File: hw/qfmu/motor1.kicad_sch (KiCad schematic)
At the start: 3 parts, among them U12 TLP2366V4-TPL_E, U3 FAN7888, U7 IMC101TT038XUMA1

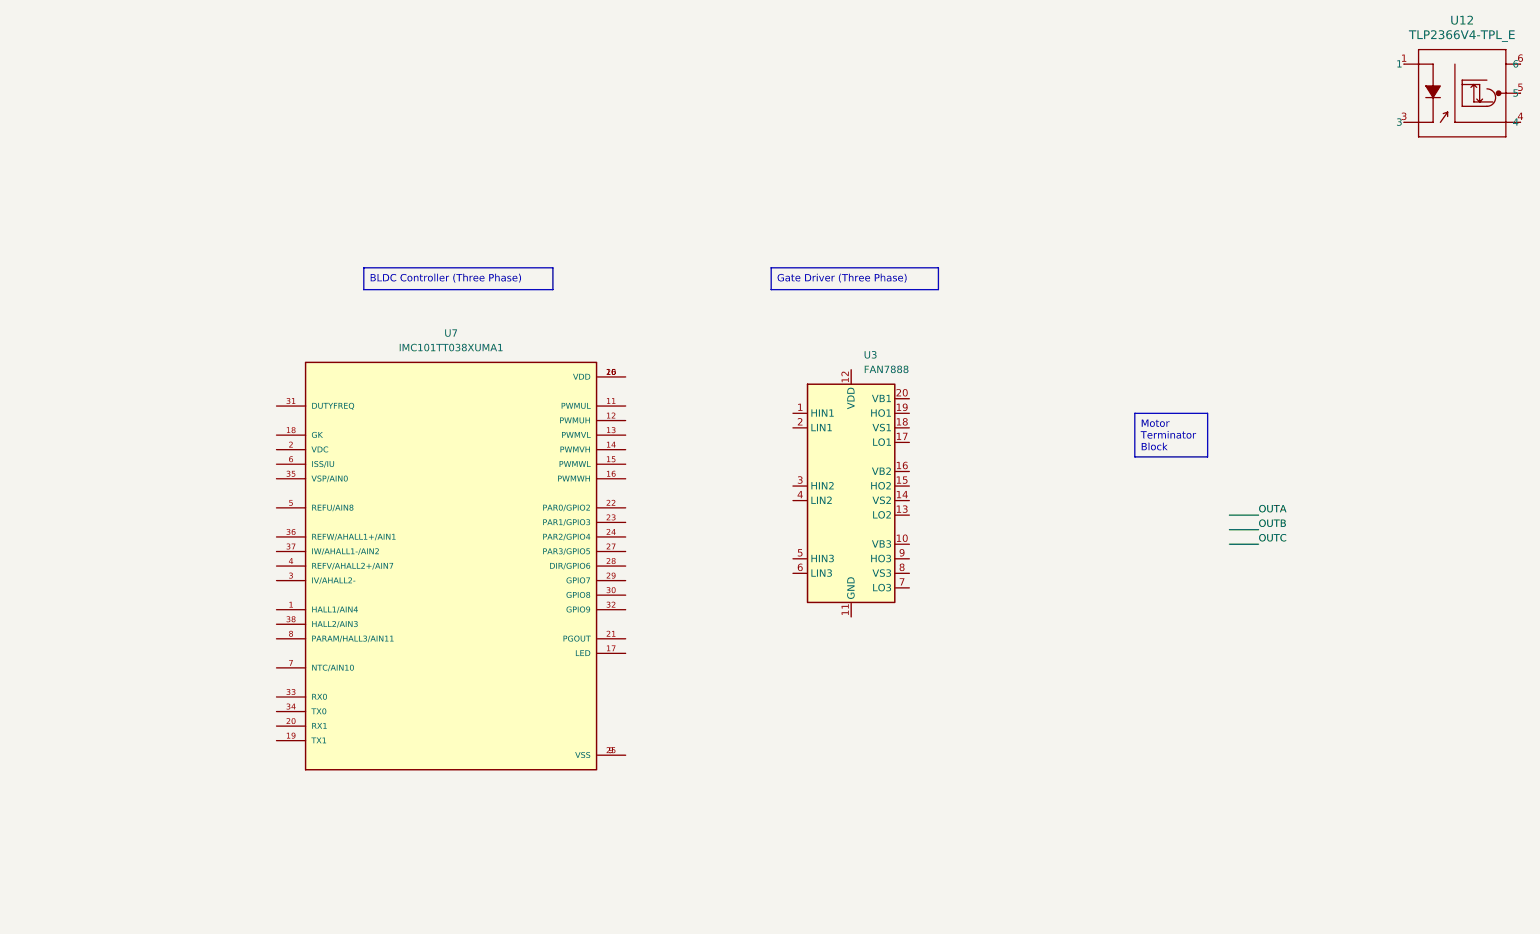
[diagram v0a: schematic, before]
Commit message: feat: add new BLDC controler and RF section
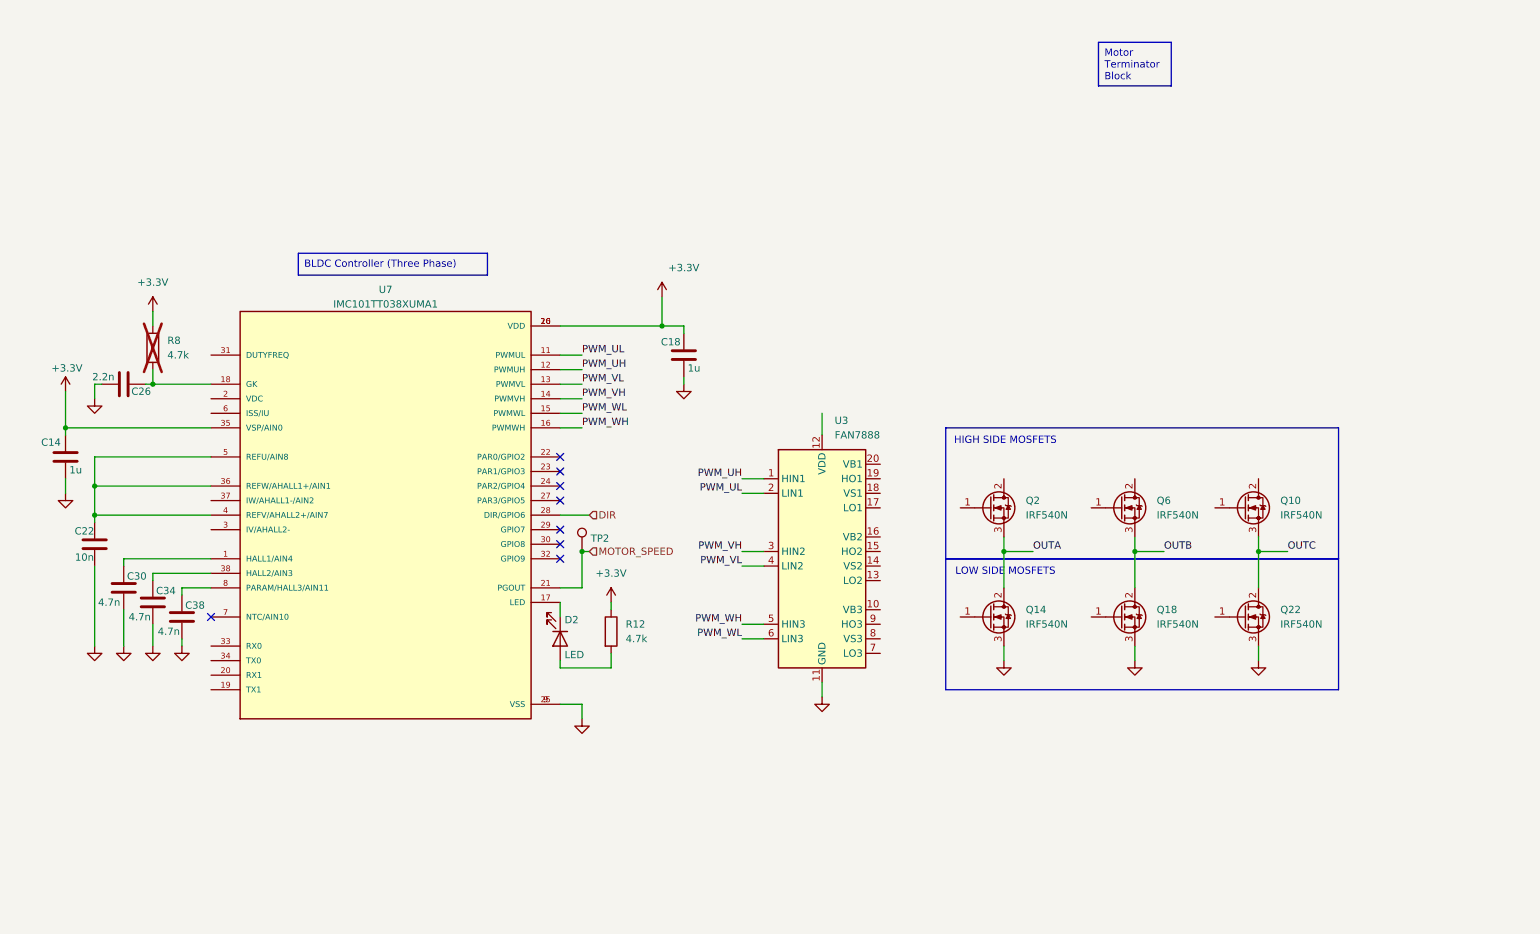
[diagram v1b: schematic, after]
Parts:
- removed U12: TLP2366V4-TPL_E, 5pin SO6_TOS, symbol TLP2366_V4_TPL_E:TLP2366V4-TPL_E
- added C14, C18: 1u, Capacitor_SMD:C_0805_2012Metric_Pad1.18x1.45mm_HandSolder, symbol Device:C
- added C22: 10n, Capacitor_SMD:C_0805_2012Metric_Pad1.18x1.45mm_HandSolder, symbol Device:C
- added C26: 2.2n, Capacitor_SMD:C_0805_2012Metric_Pad1.18x1.45mm_HandSolder, symbol Device:C
- added C30, C34, C38: 4.7n, Capacitor_SMD:C_0805_2012Metric_Pad1.18x1.45mm_HandSolder, symbol Device:C
- added D2: LED, LED_SMD:LED_1206_3216Metric_Pad1.42x1.75mm_HandSolder, symbol Device:LED
- added Q10, Q14, Q18, Q2, Q22, Q6: IRF540N, Package_TO_SOT_THT:TO-220-3_Horizontal_TabDown, symbol Transistor_FET:IRF540N
- added R12, R8: 4.7k, Resistor_SMD:R_0805_2012Metric_Pad1.20x1.40mm_HandSolder, symbol Device:R
- added TP2: TestPoint, Connector_Pin:Pin_D0.7mm_L6.5mm_W1.8mm_FlatFork, symbol Connector:TestPoint
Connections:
- net OUTA: now also Q14.2 (D), Q2.3 (S)
- net OUTB: now also Q18.2 (D), Q6.3 (S)
- net OUTC: now also Q10.3 (S), Q22.2 (D)
- net PWM_UH: now reaches U3.1 (HIN1)
- net PWM_UH: now also U7.12 (PWMUH)
- net GND: now reaches U3.11 (GND)
- net GND: now also U7.25 (VSS), U7.9 (VSS), C14.2, C18.2, C22.2, C26.1, C30.2, C34.2, C38.2, Q14.3 (S), Q18.3 (S), Q22.3 (S)
- net PWM_UL: now reaches U3.2 (LIN1)
- net PWM_UL: now also U7.11 (PWMUL)
- net PWM_VH: now reaches U3.3 (HIN2)
- net PWM_VH: now also U7.14 (PWMVH)
- net PWM_VL: now reaches U3.4 (LIN2)
- net PWM_VL: now also U7.13 (PWMVL)
- net PWM_WH: now reaches U3.5 (HIN3)
- net PWM_WH: now also U7.16 (PWMWH)
- net PWM_WL: now reaches U3.6 (LIN3)
- net PWM_WL: now also U7.15 (PWMWL)
- net at U7.1 (HALL1/AIN4): now also C30.1
- net +3.3V: now reaches U7.10 (VDD), U7.26 (VDD)
- net +3.3V: now also U7.35 (VSP/AIN0), C14.1, C18.1, R12.1, R8.1
- net at U7.17 (LED): now also D2.1 (K)
- net at U7.18 (GK): now also C26.2, R8.2
- net MOTOR_SPEED: now reaches U7.21 (PGOUT)
- net MOTOR_SPEED: now also TP2.1
- net DIR: now reaches U7.28 (DIR/GPIO6)
- net at U7.36 (REFW/AHALL1+/AIN1): now also U7.4 (REFV/AHALL2+/AIN7), U7.5 (REFU/AIN8), C22.1
- net at U7.38 (HALL2/AIN3): now also C34.1
- net at U7.8 (PARAM/HALL3/AIN11): now also C38.1
- new net: D2.2 (A), R12.2
- no-connect marks 0 -> 8
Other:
- note added: "HIGH SIDE MOSFETS"
- note added: "LOW SIDE MOSFETS"
- company: Daniel Pérez -> Daniel Enrique Pérez Díaz
- title: (none) -> Quincy FMU

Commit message: feat: finish motors, RF and power monitor
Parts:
- removed U3: FAN7888, Package_SO:SOIC-20W_7.5x12.8mm_P1.27mm, symbol Driver_FET:FAN7888
- added C74: 220p, Capacitor_SMD:C_0805_2012Metric_Pad1.18x1.45mm_HandSolder, symbol Device:C
- added C77: 1u, Capacitor_SMD:C_0805_2012Metric_Pad1.18x1.45mm_HandSolder, symbol Device:C
- added C81, C85, C89: 0.1u, Capacitor_SMD:C_0805_2012Metric_Pad1.18x1.45mm_HandSolder, symbol Device:C
- added J4: Conn_01x03_Pin, Connector_Phoenix_SPT:PhoenixContact_SPT_1.5_3-H-3.5_1x03_P3.5mm_Horizontal, symbol Connector:Conn_01x03_Pin
- added R4: 1, Resistor_SMD:R_0805_2012Metric_Pad1.20x1.40mm_HandSolder, symbol Device:R
- added R44: 2k, Resistor_SMD:R_0805_2012Metric_Pad1.20x1.40mm_HandSolder, symbol Device:R
- added R48: 10k, Resistor_SMD:R_0805_2012Metric_Pad1.20x1.40mm_HandSolder, symbol Device:R
- added R51: 100k, Resistor_SMD:R_0805_2012Metric_Pad1.20x1.40mm_HandSolder, symbol Device:R
- added R55: 300k, Resistor_SMD:R_0805_2012Metric_Pad1.20x1.40mm_HandSolder, symbol Device:R
- added U2: DRV8300UDPWR, TSSOP_0DIPWR_TEX, symbol DRV8300UDPWR:DRV8300UDPWR
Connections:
- net +3.3V: now also R48.2
- net GND: now also C74.2, C77.1, R4.2, R55.1, U2.8 (GND); no longer Q14.3 (S), Q18.3 (S), Q22.3 (S)
- net OUTA: now also C81.1, J4.3 (Pin_3), U2.18 (SHA)
- net OUTB: now also C85.1, J4.2 (Pin_2), U2.15 (SHB)
- net OUTC: now also C89.1, J4.1 (Pin_1), U2.12 (SHC)
- net PWM_UH: now also U2.1 (INHA)
- net PWM_UL: now also U2.4 (INLA)
- net PWM_VH: now also U2.2 (INHB)
- net PWM_VL: now also U2.5 (INLB)
- net PWM_WH: now also U2.3 (INHC)
- net PWM_WL: now also U2.6 (INLC)
- net LO3: now reaches Q22.1 (G)
- net LO3: now also U2.10 (GLB)
- net HO3: now reaches Q10.1 (G)
- net HO3: now also U2.13 (GHC)
- net +12V: now reaches Q10.2 (D)
- net +12V: now also Q2.2 (D), Q6.2 (D), C77.2, R51.1, U2.7 (GVDD)
- net HO2: now reaches Q6.1 (G)
- net HO2: now also U2.16 (GHB)
- net LO2: now reaches Q18.1 (G)
- net LO2: now also U2.9 (GLC)
- net LO1: now reaches Q14.1 (G)
- net LO1: now also U2.11 (GLA)
- net HO1: now reaches Q2.1 (G)
- net HO1: now also U2.19 (GHA)
- net VDC: now reaches U7.2 (VDC)
- net VDC: now also R51.2, R55.2
- net DUTYFREQ: now reaches U7.31 (DUTYFREQ)
- net CONT_FW_RX0: now reaches U7.33 (RX0)
- net CONT_FW_TX0: now reaches U7.34 (TX0)
- net IU+: now reaches U7.6 (ISS/IU)
- net IU+: now also C74.1, R44.2, R48.1
- new net: Q14.3 (S), Q18.3 (S), Q22.3 (S), R4.1, R44.1
- new net BSTA: C81.2, U2.20 (BSTA)
- new net BSTB: C85.2, U2.17 (BSTB)
- new net BSTC: C89.2, U2.14 (BSTC)
- no-connect marks 8 -> 12
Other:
- moved on the sheet: C14, C18, C22, C26, C30, C34, C38, D2, Q10, Q14, Q18, Q2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

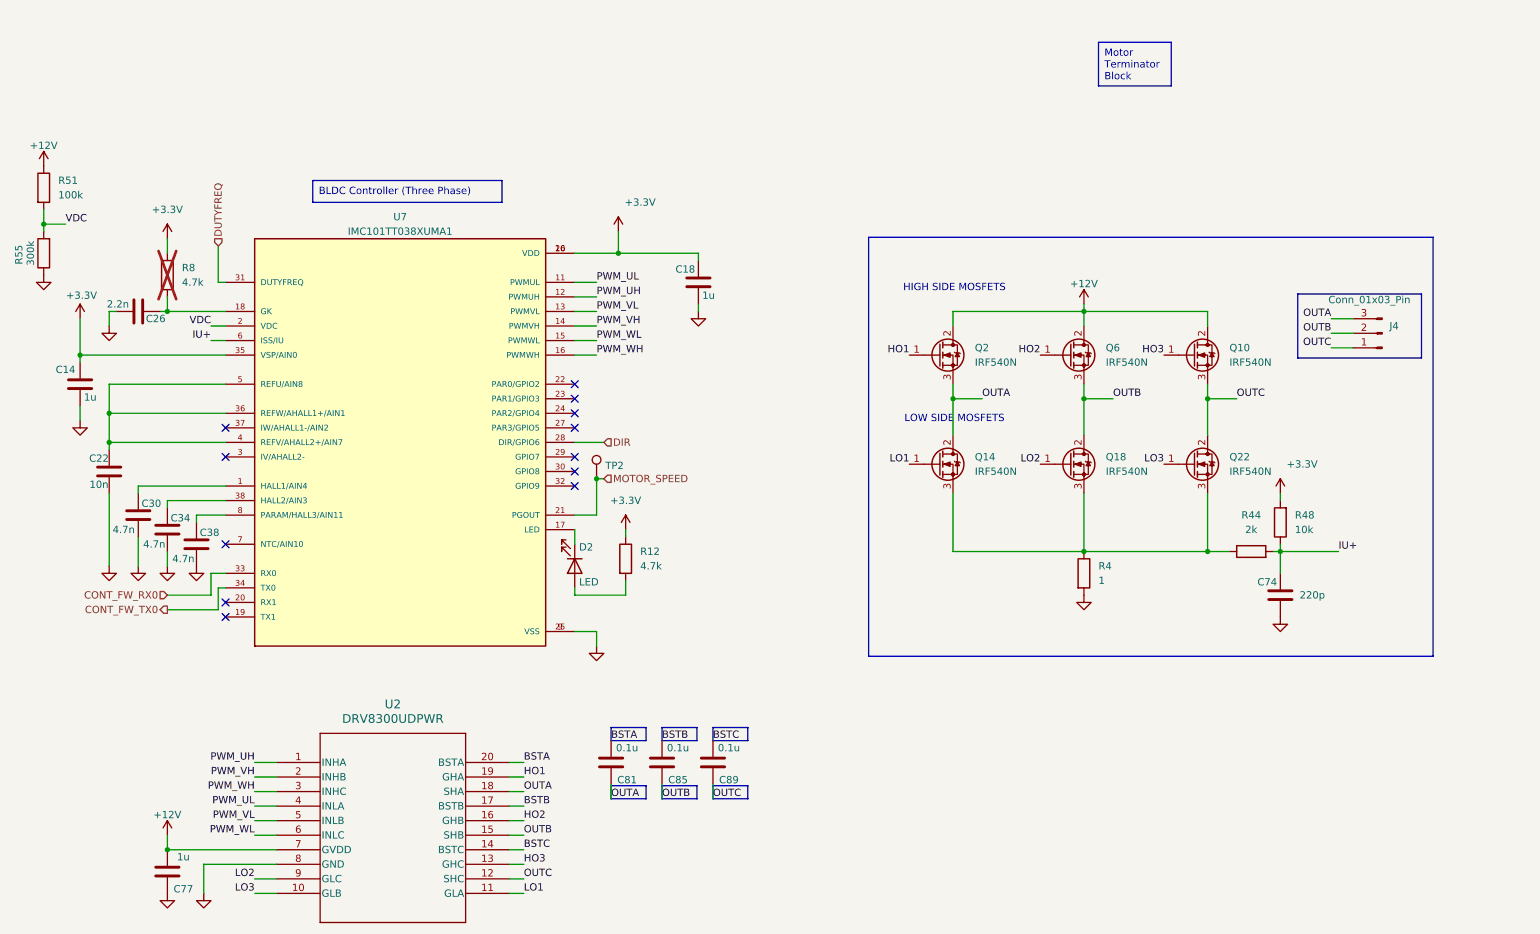
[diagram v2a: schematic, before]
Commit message: feat: start PCB design, define board outline and basic placement
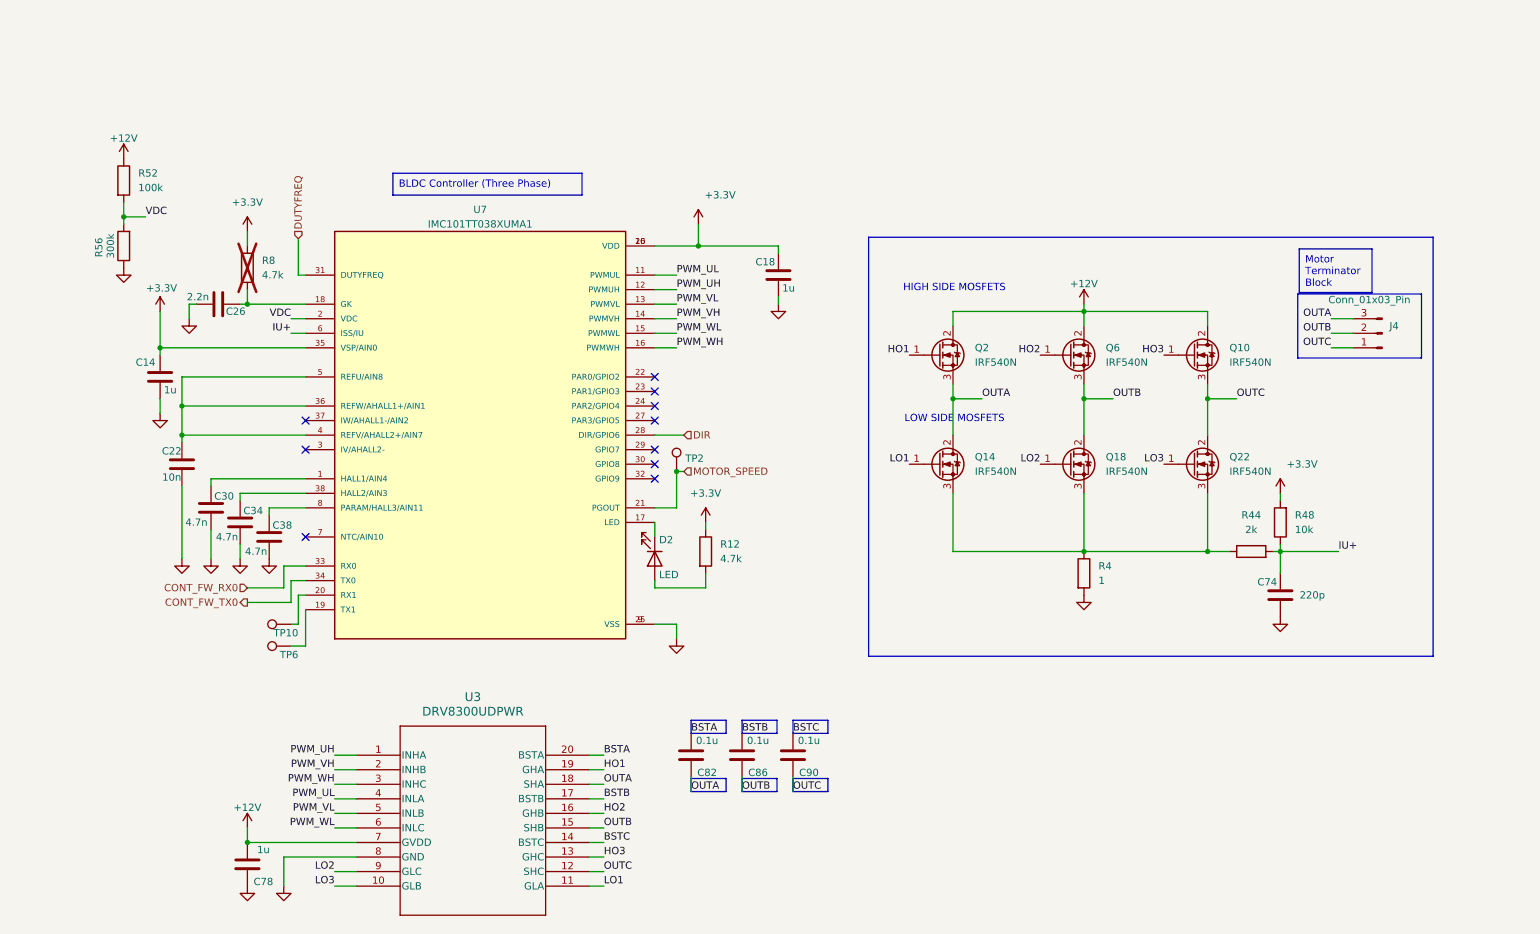
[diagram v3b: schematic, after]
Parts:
- added TP10, TP6: TestPoint, Connector_Pin:Pin_D0.7mm_L6.5mm_W1.8mm_FlatFork, symbol Connector:TestPoint
- renumbered C77 to C78, C81 to C82, C85 to C86, C89 to C90, R51 to R52, R55 to R56, U2 to U3
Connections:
- net at U7.19 (TX1): now also TP6.1
- net at U7.20 (RX1): now also TP10.1
- no-connect marks 12 -> 10
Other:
- moved on the sheet: C14, C18, C22, C26, C30, C34, C38, C78, C82, C86, C90, D2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

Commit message: feat: complete preliminar placement of PCB components
Organize and place components for routing and export a preliminary BOM
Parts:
- R8: now left out of the parts list
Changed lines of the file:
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@@
 		(at 54.61 59.69 0)
 		(unit 1)
-		(exclude_from_sim no)
-		(in_bom yes)
-		(on_board yes)
+		(exclude_from_sim yes)
+		(in_bom no)
+		(on_board no)
 		(dnp yes)
 		(fields_autoplaced yes)
